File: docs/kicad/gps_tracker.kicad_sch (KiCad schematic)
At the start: 13 parts, among them J1 GNSS: Foxeer M10Q-250 / Beiti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, J2 BIGGA GSM (SIM800C) board, J3 SSD1306 0.96" OLED I2C 0x3C, J4 MicroSD SPI module, J5 Battery Shield V8, 2x18650, J6 BMA400 CJMCU-400 (not fitted 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, SW1 Button (BOOT-style, active lo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, U1 ESP32-S3-WROOM-1 (DevKitC-1)

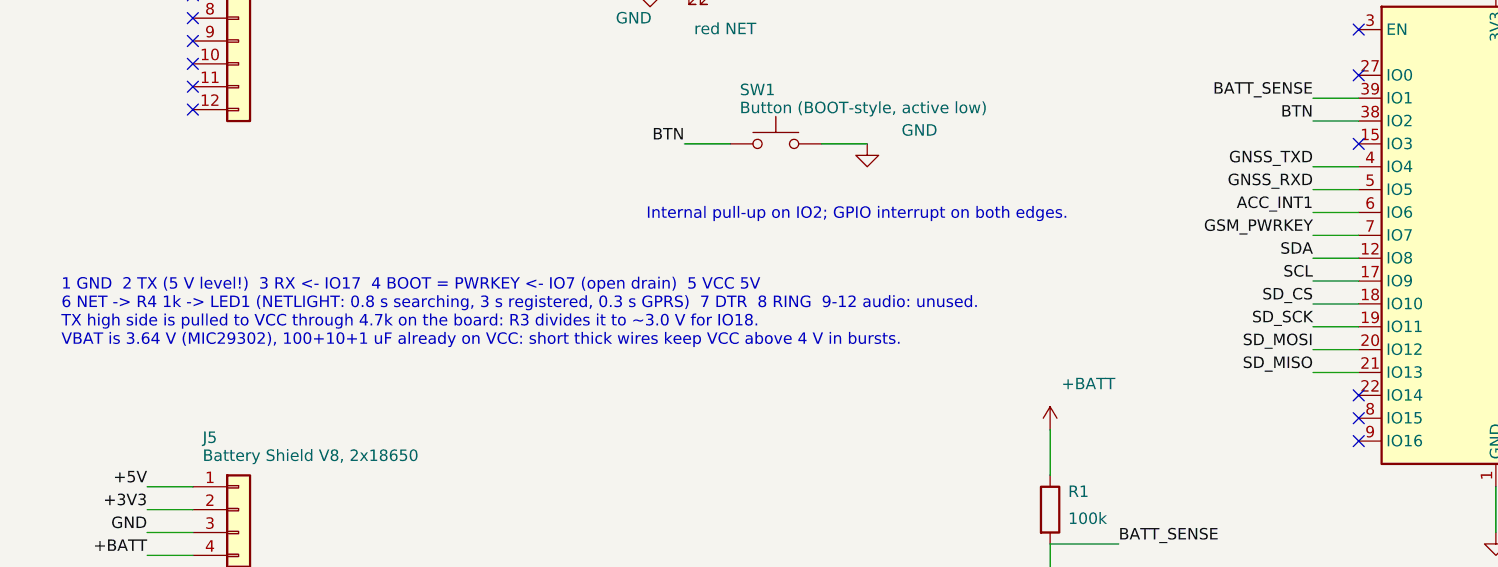
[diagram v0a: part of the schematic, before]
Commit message: BIGGA GSM: use the board's silkscreen names (NET VSS PK RX TX GND)
The delivered board labels the six wired pins NET, VSS, PK, RX, TX, GND:
the schematic's header read from the other end, with VSS meaning the 5 V
supply input (not ground, as the name usually implies) and PK the power
key. Sheet, wiring diagram, schematic note and hardware doc now show the
silkscreen names next to the schematic ones, with the VSS warning and a
continuity check against the SMA shell.
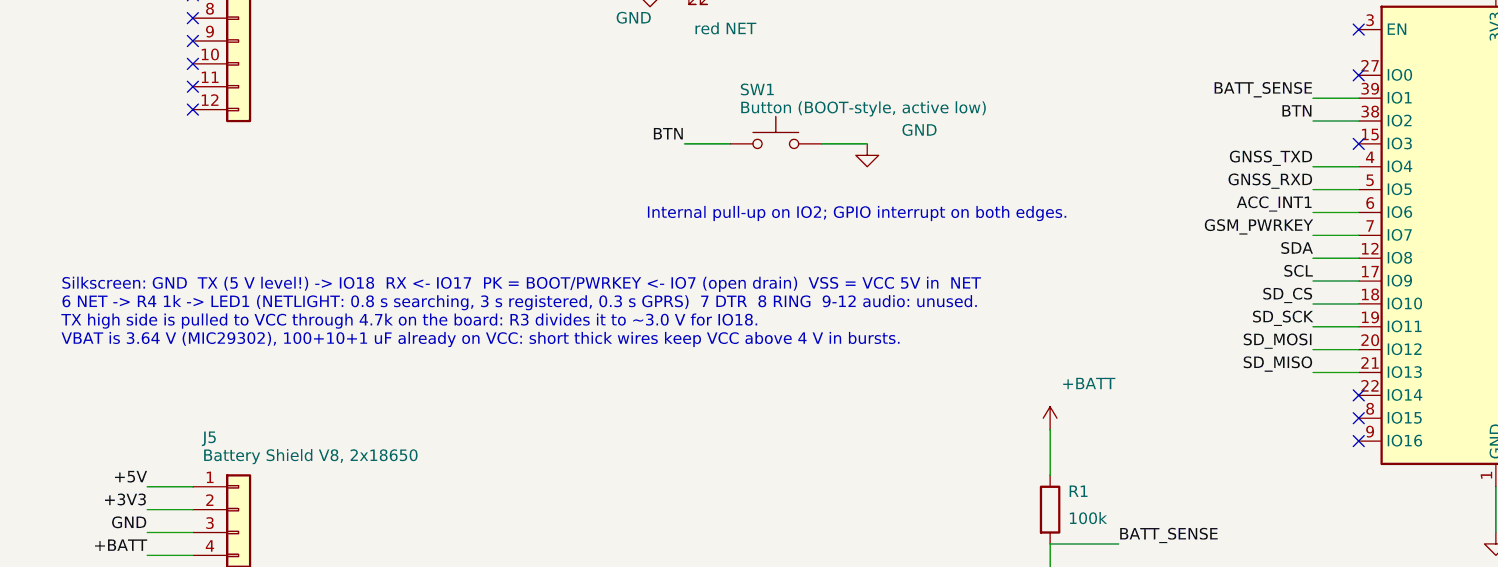
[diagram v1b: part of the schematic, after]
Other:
- note added: "Silkscreen: GND TX (5 V level!) -> IO18 RX <- IO17 PK = BOOT/PWRKEY <- IO7 (open drain) VSS = VCC 5V in NET 6 NET -> R4 1k -> LED1 (NETLIGHT: 0.8 s searching, 3 s registered, 0.3 s GPRS) 7 DTR 8 RING 9-12 audio: unused. TX high side is pulled to VCC through 4.7k on the board: R3 divides it to ~3.0 V for IO18. VBAT is 3.64 V (MIC29302), 100+10+1 uF already on VCC: short thick wires keep VCC above 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"
- note removed: "1 GND 2 TX (5 V level!) 3 RX <- IO17 4 BOOT = PWRKEY <- IO7 (open drain) 5 VCC 5V 6 NET -> R4 1k -> LED1 (NETLIGHT: 0.8 s searching, 3 s registered, 0.3 s GPRS) 7 DTR 8 RING 9-12 audio: unused. TX high side is pulled to VCC through 4.7k on the board: R3 divides it to ~3.0 V for IO18. VBAT is 3.64 V (MIC29302), 100+10+1 uF already on VCC: short thick wires keep VCC above 4 V in bursts."

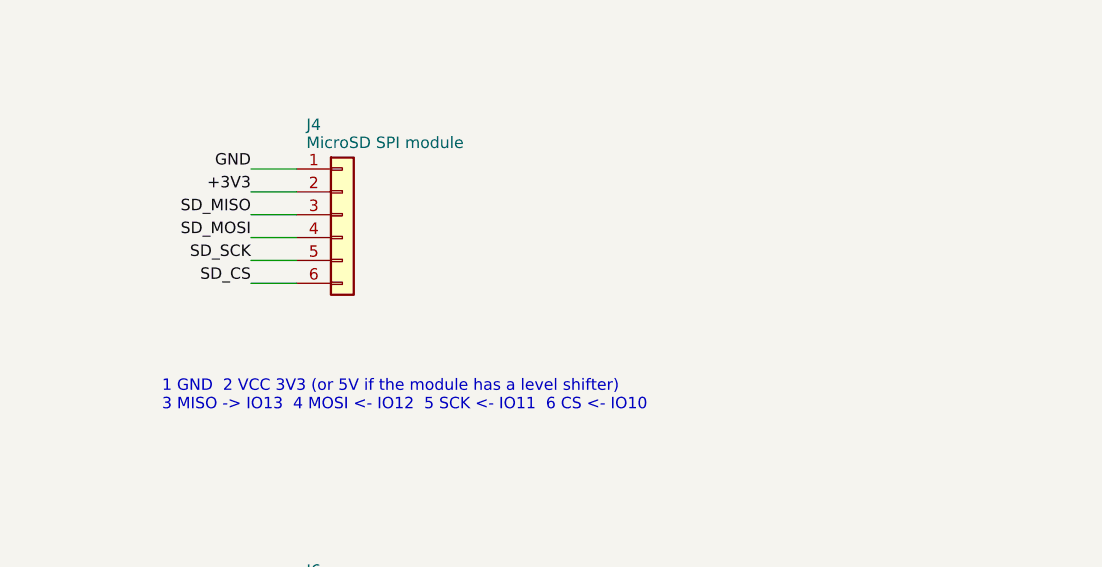
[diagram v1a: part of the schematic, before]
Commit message: MicroSD adapter is the 5 V type: VCC on the 5 V rail
The adapter in use is the six-pin board rated 4.5-5.5 V, with its own
3.3 V regulator and level shifter. On the 3 V rail it stays silent and the
firmware logs a mount timeout at boot, which is what was observed. Sheet,
wiring diagram, schematic, hardware doc, README and the config comment now
put its VCC on +5V unconditionally.
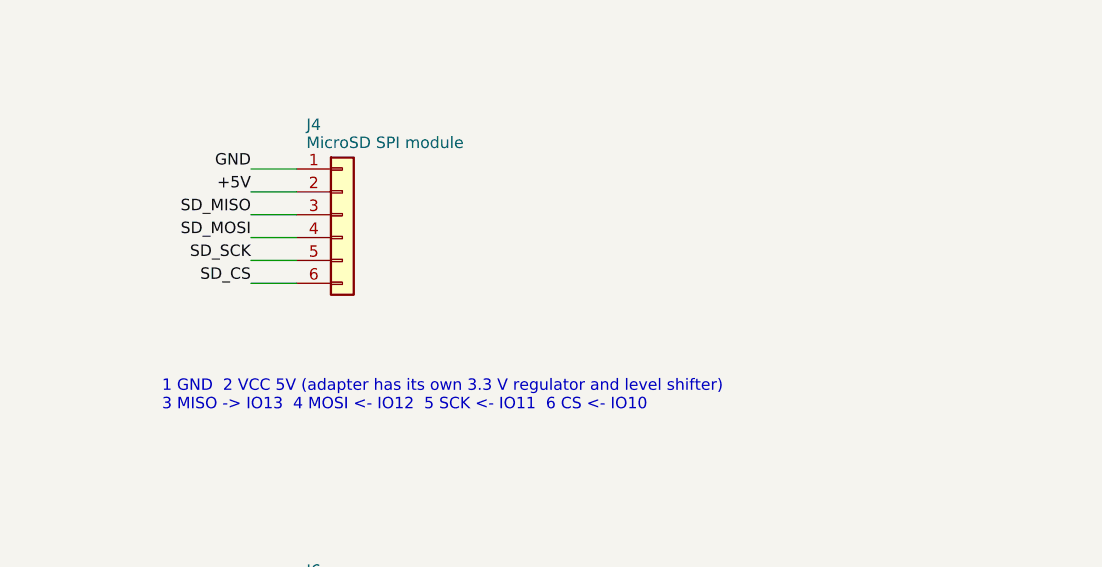
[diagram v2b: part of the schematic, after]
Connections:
- net +3V3: no longer J4.2 (Pin_2)
- net +5V: now also J4.2 (Pin_2)
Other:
- note added: "1 GND 2 VCC 5V (adapter has its own 3.3 V regulator and level shifter) 3 MISO -> IO13 4 MOSI <- IO12 5 SCK <- IO11 6 CS <- IO10"
- note removed: "1 GND 2 VCC 3V3 (or 5V if the module has a level shifter) 3 MISO -> IO13 4 MOSI <- IO12 5 SCK <- IO11 6 CS <- IO10"

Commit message: GNSS UART pins swapped: receiver TX to GPIO5, RX to GPIO4
Straight wiring on the breadboard: the receiver's TX now lands on GPIO5
and its RX on GPIO4, so the two jumpers no longer cross. Config, GPIO
map, wiring diagram, assembly sheet and the KiCad schematic (ERC 0/0)
are regenerated together so every drawing matches the firmware.
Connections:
- net GNSS_RXD: now also U1.4 (IO4); no longer U1.5 (IO5)
- net GNSS_TXD: now also U1.5 (IO5); no longer U1.4 (IO4)
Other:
- note added: "1 VCC 5V 2 GND 3 TX -> IO5 4 RX <- IO4 5 SCL / 6 SDA: compass (Foxeer only, 0x0D). BE-220 has pins 1-4."
- note removed: "1 VCC 5V 2 GND 3 TX -> IO4 4 RX <- IO5 5 SCL / 6 SDA: compass (Foxeer only, 0x0D). BE-220 has pins 1-4."

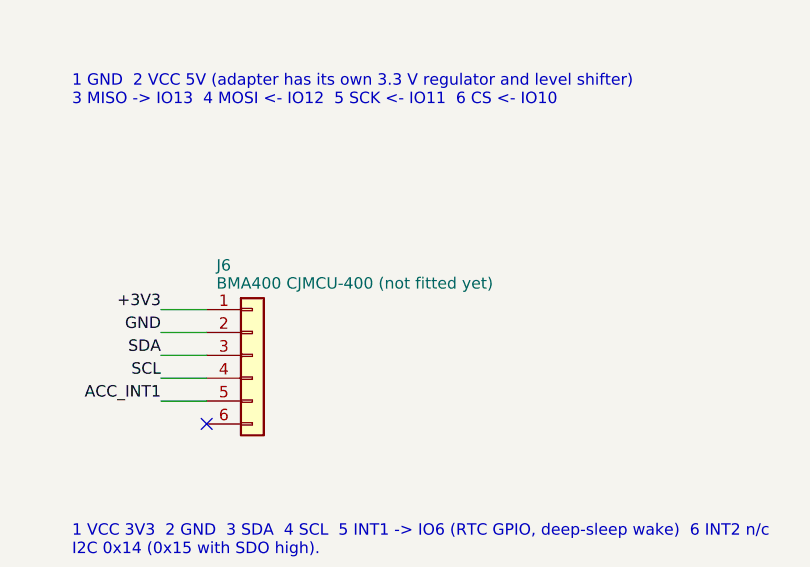
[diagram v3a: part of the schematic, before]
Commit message: BMA400 motion source: the accelerometer decides moving/parked
The CJMCU-400 arrived, so the slot reserved for it is filled. Bma400
(periph) probes 0x14 and 0x15 for the chip id, soft-resets, and
configures generic interrupt 1 for activity: a change between
consecutive samples above 96 mg on any axis, sustained for 10 samples at
100 Hz, pulsed on INT1 (GPIO6). The ISR only counts pulses; no I2C
traffic after begin(), so the bus stays the display's at run time.

AccelMotionDetector (logic) implements IMotionDetector from an
IActivitySource: moving on the first pulse, stopped after
motion_stop_delay_ms without one. It needs no fix and is immune to the
position noise that made the speed detector flap at a window. App points
motion_ at it when the chip answers at boot and falls back to GNSS speed
otherwise; the diagnostics line names the source and the pulse count.
Two host tests cover start, restart inside the delay, stop, and
independence from the fix.

Docs, wiring diagram, assembly sheet and schematic (ERC 0/0) now show
the BMA400 as fitted; deep sleep remains the next step.
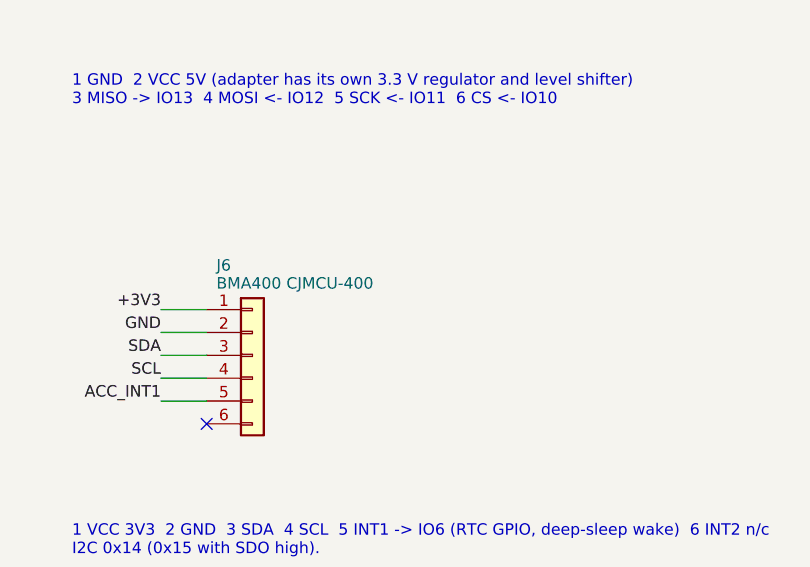
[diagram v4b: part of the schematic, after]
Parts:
- J6: value BMA400 CJMCU-400 (not fitted yet) -> BMA400 CJMCU-400
